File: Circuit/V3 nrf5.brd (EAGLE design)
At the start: 41 x 64.5 mm, 77 parts, among them J4 USB Micro, J7 CORTEX_DEBUG_SMD, Q1 FDV301N, Q2 BSS84, U1 AL8805, U2 MCP73831, U3 BC840M, U4 3.3V/150mA, U5 AL8805, U6 AL8805, U8 TPS61236P, Y1 32.768kHz

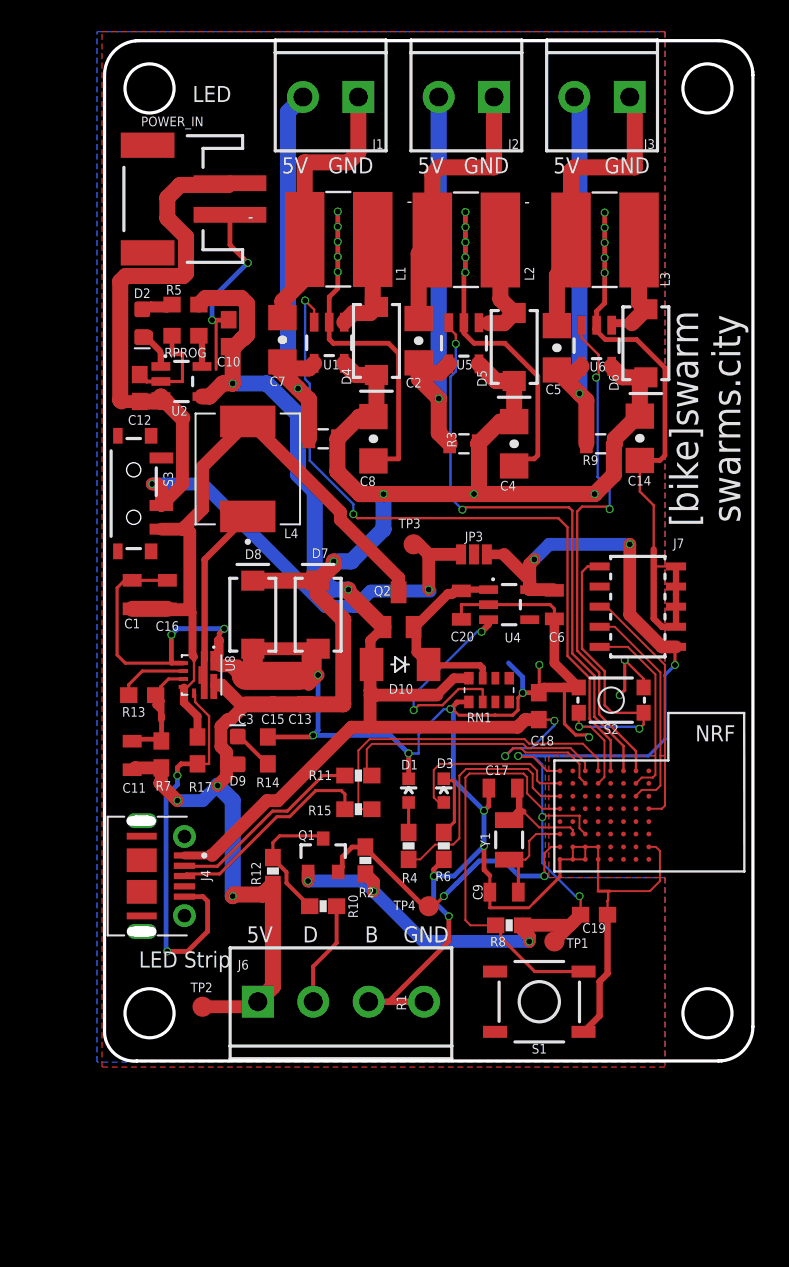
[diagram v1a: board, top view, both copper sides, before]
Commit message: clean traces
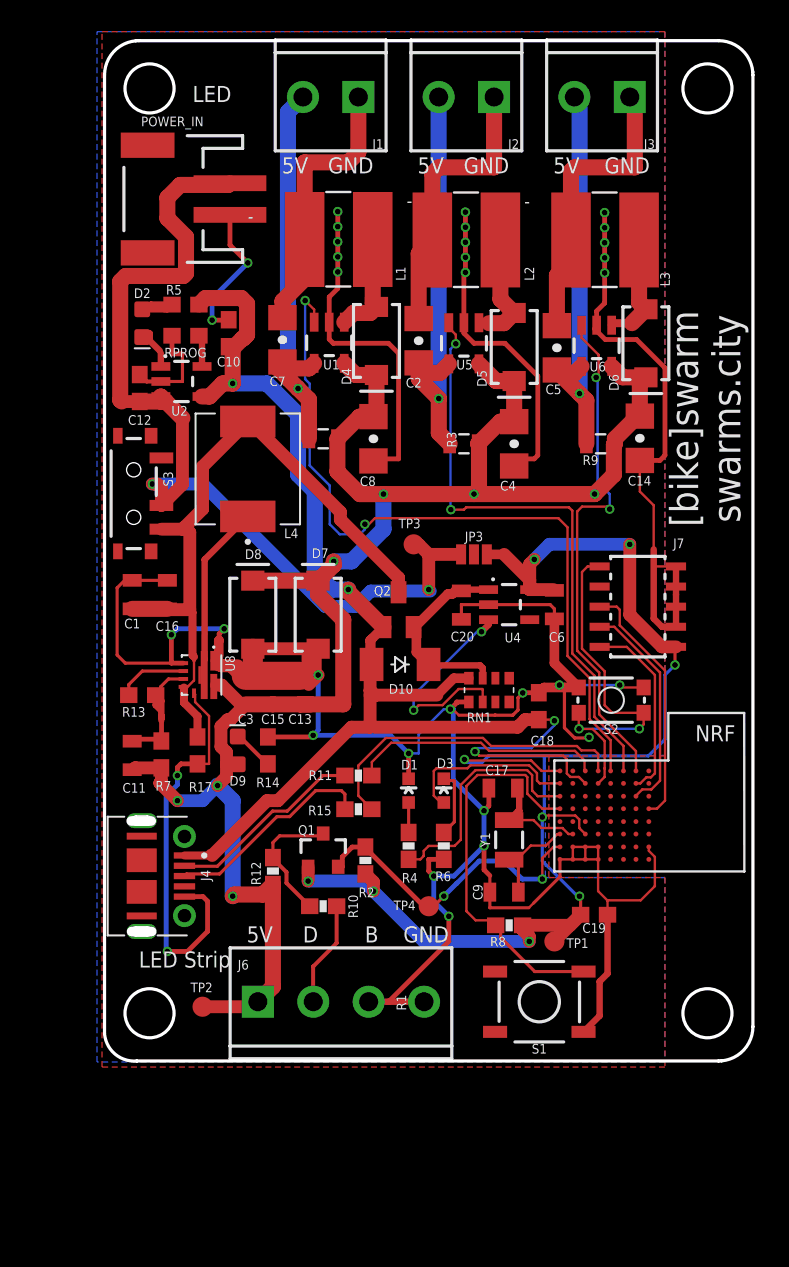
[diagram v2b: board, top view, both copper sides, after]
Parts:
- moved Q1 0.32 mm to (14.0, 13.7)
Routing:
- net GND: track 300.9 -> 292.4 mm, vias 34 -> 33
- net 3.3V: track 81.2 -> 88.0 mm
- net VBUS: track 90.8 -> 94.3 mm
- net CTRL_CH1: track 46.7 -> 49.0 mm
- net SWITCH_1: track 25.9 -> 24.9 mm
- net D+: track 21.3 -> 20.5 mm
- net SWO: track 15.6 -> 16.3 mm
- net LED_2: track 11.9 -> 11.2 mm

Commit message: traces
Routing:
- net VBAT_S: track 65.4 -> 64.7 mm
- net N$3: track 12.8 -> 13.4 mm
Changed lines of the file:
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@@
 <via x="22.0345" y="35.21075" extent="1-16" drill="0.35"/>
 <wire x1="22.0091" y1="35.23615" x2="22.0345" y2="35.21075" width="0.1524" layer="16"/>
-<wire x1="23.00605" y1="35.3568" x2="22.86" y2="35.21075" width="0.1524" layer="1"/>
-<wire x1="22.0345" y1="35.21075" x2="22.86" y2="35.21075" width="0.1524" layer="1"/>
-<wire x1="23.00605" y1="35.3568" x2="29.49500625" y2="35.3568" width="0.1524" layer="1"/>
-<wire x1="29.49500625" y1="35.3568" x2="29.7084" y2="35.14340625" width="0.1524" layer="1"/>
+<wire x1="22.0345" y1="35.21075" x2="29.4005" y2="35.21075" width="0.1524" layer="1"/>
+<wire x1="29.4005" y1="35.21075" x2="29.7084" y2="34.90285" width="0.1524" layer="1"/>
+<wire x1="29.7084" y1="34.90285" x2="29.7084" y2="26.11794375" width="0.1524" layer="1"/>
 <wire x1="29.7084" y1="26.11794375" x2="31.1023" y2="24.72404375" width="0.1524" layer="1"/>
-<wire x1="29.7084" y1="35.14340625" x2="29.7084" y2="26.11794375" width="0.1524" layer="1"/>
 <wire x1="31.1023" y1="22.1230625" x2="31.1023" y2="24.72404375" width="0.1524" layer="1"/>
 <contactref element="U3" pad="A2"/>
@@
 <wire x1="3.7465" y1="18.8985" x2="2.109" y2="18.8985" width="0.8128" layer="1"/>
 <via x="14.63675" y="31.9405" extent="1-16" drill="0.35"/>
-<wire x1="17.78" y1="33.9725" x2="15.748" y2="31.9405" width="1.016" layer="16"/>
-<wire x1="14.63675" y1="31.9405" x2="15.748" y2="31.9405" width="1.016" layer="16"/>
+<wire x1="17.78" y1="33.9725" x2="16.5735" y2="32.766" width="1.016" layer="16"/>
+<wire x1="14.63675" y1="31.9405" x2="14.63675" y2="32.73425" width="1.016" layer="16"/>
+<wire x1="14.6685" y1="32.766" x2="14.63675" y2="32.73425" width="1.016" layer="16"/>
+<wire x1="16.5735" y1="32.766" x2="14.6685" y2="32.766" width="1.016" layer="16"/>
 <wire x1="17.78" y1="33.9725" x2="17.78" y2="36.195" width="1.016" layer="16"/>
 <via x="17.78" y="36.195" extent="1-16" drill="0.35"/>
@@
 <wire x1="6.4565" y1="25.7175" x2="6.4565" y2="27.305" width="0.3048" layer="1"/>
 <wire x1="6.4565" y1="27.305" x2="6.5165" y2="27.365" width="0.3048" layer="1"/>
-<wire x1="9.2075" y1="34.7825" x2="6.4809" y2="32.0559" width="0.4064" layer="1"/>
+<wire x1="9.2075" y1="34.7825" x2="8.255" y2="34.7825" width="0.4064" layer="1"/>
+<wire x1="8.255" y1="34.7825" x2="6.4809" y2="33.0084" width="0.4064" layer="1"/>
 <wire x1="6.4809" y1="25.7419" x2="6.4565" y2="25.7175" width="0.4064" layer="1"/>
-<wire x1="6.4809" y1="32.0559" x2="6.4809" y2="25.7419" width="0.4064" layer="1"/>
+<wire x1="6.4809" y1="33.0084" x2="6.4809" y2="25.7419" width="0.4064" layer="1"/>
 </signal>
 <signal name="N$8">
@@
 <wire x1="1.1494" y1="42.13490625" x2="1.24480625" y2="42.0395" width="0.8128" layer="1"/>
 <wire x1="1.24480625" y1="42.0395" x2="2.386" y2="42.0395" width="0.8128" layer="1"/>
-<wire x1="3.75025" y1="35.47675" x2="3.75025" y2="36.57225" width="0.8128" layer="1"/>
-<wire x1="3.75025" y1="36.57225" x2="3.4925" y2="36.83" width="0.8128" layer="1"/>
-<wire x1="3.4925" y1="36.83" x2="3.175" y2="36.83" width="0.8128" layer="1"/>
-<via x="3.175" y="36.83" extent="1-16" drill="0.35"/>
+<wire x1="3.84175" y1="37.05225" x2="3.75025" y2="36.96075" width="0.8128" layer="1"/>
+<wire x1="3.75025" y1="36.96075" x2="3.75025" y2="35.47675" width="0.8128" layer="1"/>
+<via x="3.84175" y="37.05225" extent="1-16" drill="0.35"/>
 <wire x1="14.09824375" y1="29.0957" x2="15.9993875" y2="29.0957" width="0.8128" layer="16"/>
-<wire x1="3.175" y1="36.83" x2="6.36394375" y2="36.83" width="0.8128" layer="16"/>
+<wire x1="3.84175" y1="37.05225" x2="6.14169375" y2="37.05225" width="0.8128" layer="16"/>
 <wire x1="16.9709375" y1="30.06725" x2="20.73275" y2="30.06725" width="0.8128" layer="16"/>
-<wire x1="6.36394375" y1="36.83" x2="14.09824375" y2="29.0957" width="0.8128" layer="16"/>
+<wire x1="6.14169375" y1="37.05225" x2="14.09824375" y2="29.0957" width="0.8128" layer="16"/>
 <wire x1="15.9993875" y1="29.0957" x2="16.9709375" y2="30.06725" width="0.8128" layer="16"/>
 <wire x1="20.6375" y1="32.385" x2="20.6375" y2="30.1625" width="0.8128" layer="1"/>

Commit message: Updating digikey parts.
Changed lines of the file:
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@@
 <drawing>
 <settings>
-<setting alwaysvectorfont="no"/>
+<setting alwaysvectorfont="yes"/>
 <setting keepoldvectorfont="yes"/>
 <setting verticaltext="up"/>
@@
 <layer number="25" name="tNames" color="7" fill="1" visible="yes" active="yes"/>
 <layer number="26" name="bNames" color="7" fill="1" visible="yes" active="yes"/>
-<layer number="27" name="tValues" color="7" fill="1" visible="no" active="yes"/>
+<layer number="27" name="tValues" color="7" fill="1" visible="yes" active="yes"/>
 <layer number="28" name="bValues" color="7" fill="1" visible="no" active="yes"/>
 <layer number="29" name="tStop" color="7" fill="3" visible="no" active="yes"/>
@@
 </element>
 <element name="R10" library="SparkFun" package="0603-RES" value="330" x="13.97" y="10.16" smashed="yes" rot="R180">
-<attribute name="DIGIKEY" value="A130088CT-ND" x="13.97" y="10.16" size="1.778" layer="27" rot="R180" display="off"/>
+<attribute name="DIGIKEY" value="P330HCT-ND" x="13.97" y="10.16" size="1.778" layer="27" rot="R180" display="off"/>
 <attribute name="NAME" x="15.5575" y="10.89025" size="0.6096" layer="25" font="vector" rot="R270"/>
 <attribute name="VALUE" x="14.986" y="11.303" size="0.4064" layer="27" font="vector" rot="R180"/>
@@
 </element>
 <element name="R15" library="SparkFun" package="0603-RES" value="22" x="16.1925" y="16.28775" smashed="yes">
-<attribute name="DIGIKEY" value="P10KGCT-ND" x="16.1925" y="16.28775" size="1.778" layer="27" display="off"/>
+<attribute name="DIGIKEY" value="A103067TR-ND " x="16.1925" y="16.28775" size="1.778" layer="27" display="off"/>
 <attribute name="NAME" x="13.0175" y="15.90675" size="0.6096" layer="25" font="vector"/>
 <attribute name="VALUE" x="15.1765" y="15.14475" size="0.4064" layer="27" font="vector"/>
@@
 <wire x1="7.374" y1="26.935" x2="7.374" y2="25.9825" width="0.6096" layer="1"/>
 <wire x1="7.374" y1="25.9825" x2="7.0565" y2="25.665" width="0.3048" layer="1"/>
-<wire x1="6.0325" y1="19.1525" x2="4.98475" y2="19.1525" width="0.3048" layer="1"/>
-<wire x1="4.7625" y1="18.415" x2="4.7625" y2="18.93025" width="0.3048" layer="1"/>
-<wire x1="4.98475" y1="19.1525" x2="4.7625" y2="18.93025" width="0.3048" layer="1"/>
-<via x="4.7625" y="18.415" extent="1-16" drill="0.35"/>
-<wire x1="4.7625" y1="18.415" x2="4.7625" y2="17.83329375" width="0.3048" layer="16"/>
-<wire x1="4.7625" y1="17.83329375" x2="4.0513" y2="17.12209375" width="0.3048" layer="16"/>
+<wire x1="6.0325" y1="19.1525" x2="6.0325" y2="15.875" width="0.3048" layer="1"/>
+<via x="6.0325" y="15.875" extent="1-16" drill="0.35"/>
+<wire x1="6.0325" y1="15.875" x2="4.7625" y2="15.875" width="0.3048" layer="16"/>
+<wire x1="4.7625" y1="15.875" x2="4.0513" y2="15.1638" width="0.3048" layer="16"/>
+<wire x1="4.0513" y1="15.1638" x2="4.0513" y2="7.3787" width="0.3048" layer="16"/>
 <via x="4.1275" y="7.3025" extent="1-16" drill="0.35"/>
 <wire x1="4.1275" y1="7.3025" x2="5.3975" y2="7.3025" width="0.3048" layer="1"/>
@@
 <wire x1="6.6675" y1="10.4775" x2="6.38" y2="10.765" width="0.3048" layer="1"/>
 <wire x1="6.38" y1="10.765" x2="5.2075" y2="10.765" width="0.3048" layer="1"/>
-<wire x1="4.0513" y1="17.12209375" x2="4.0513" y2="7.3787" width="0.3048" layer="16"/>
 <wire x1="4.0513" y1="7.3787" x2="4.1275" y2="7.3025" width="0.3048" layer="16"/>
 <wire x1="8.001" y1="47.205" x2="7.9765" y2="47.1805" width="0.3048" layer="1"/>

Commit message: Changing pins to match board.
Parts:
- U4: value 3.3V/150mA -> MIC5205
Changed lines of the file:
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@@
 <attribute name="VALUE" x="21.87575" y="27.84475" size="1.27" layer="27" rot="R180"/>
 </element>
-<element name="U4" library="SparkFun-IC-Power" library_urn="urn:adsk.eagle:library:526" package="SOT23-5" package3d_urn="urn:adsk.eagle:package:39060/1" value="3.3V/150mA" x="25.7175" y="29.21" smashed="yes" rot="R270">
+<element name="U4" library="SparkFun-IC-Power" library_urn="urn:adsk.eagle:library:526" package="SOT23-5" package3d_urn="urn:adsk.eagle:package:39060/1" value="MIC5205" x="25.7175" y="29.21" smashed="yes" rot="R270">
 <attribute name="DIGIKEY" value="576-1259-1-ND" x="25.7175" y="29.21" size="1.778" layer="27" rot="R270" display="off"/>
 <attribute name="NAME" x="25.43175" y="26.82875" size="0.6096" layer="25"/>

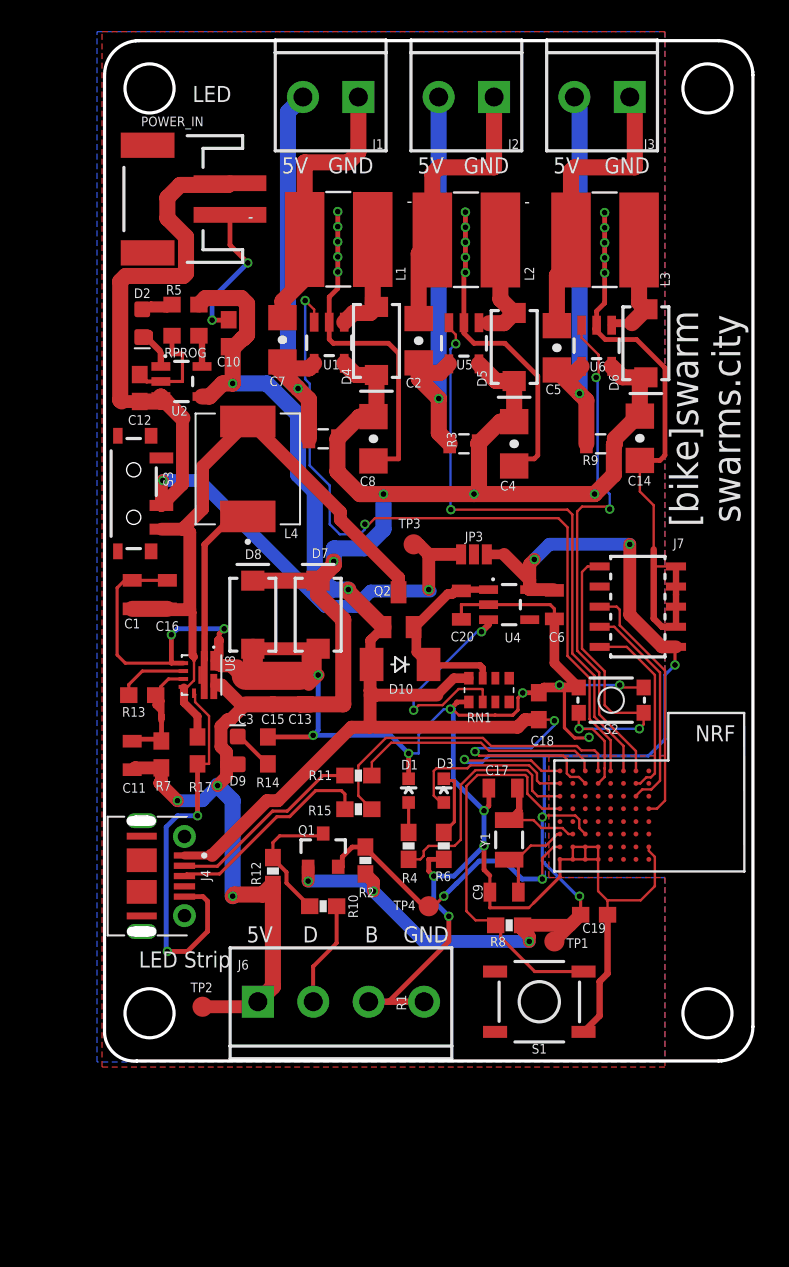
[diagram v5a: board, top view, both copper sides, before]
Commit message: Removing picobuck, touching up and finalizing schematic layout, switching to neopixel 3W led (headlamp). Needs new dimensions to fit with battery in enclosure.
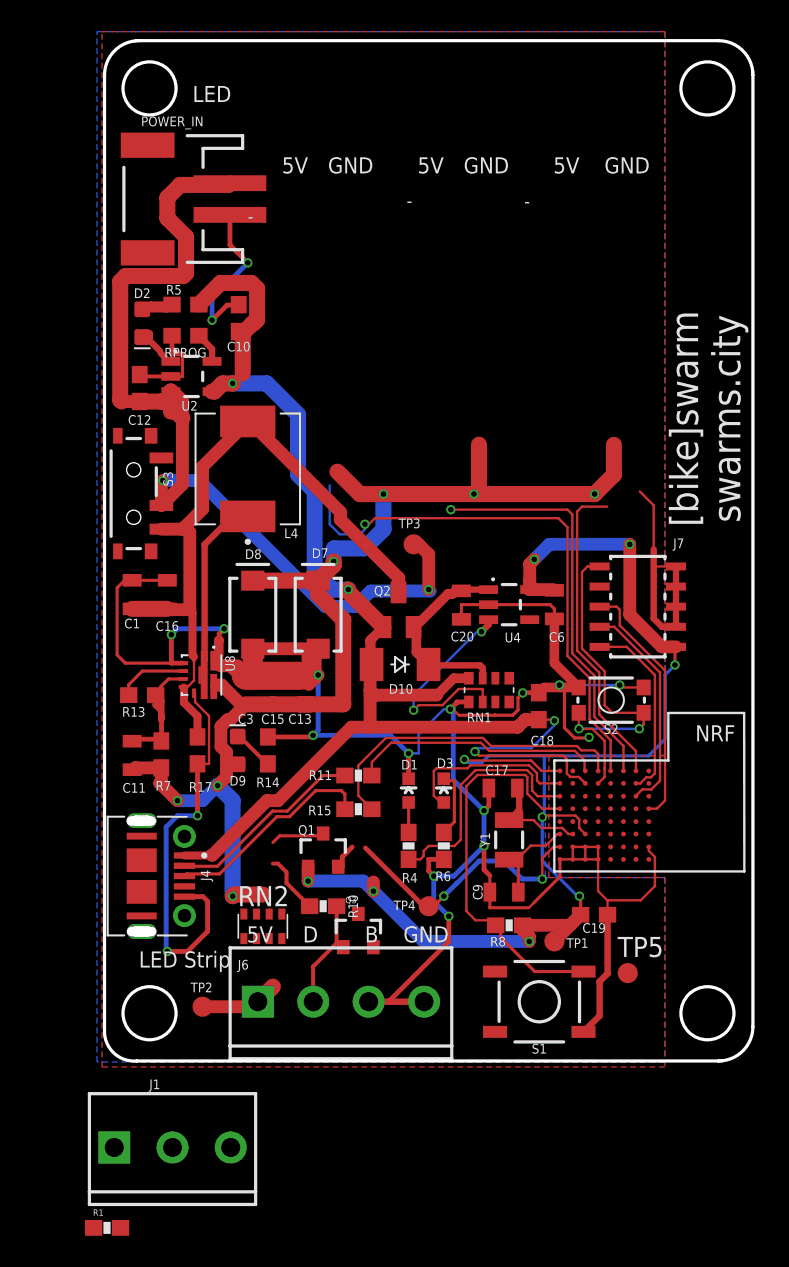
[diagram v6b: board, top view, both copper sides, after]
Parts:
- removed C14, C4, C8: 2.2uF, SparkFun-Capacitors:1206-CAP
- removed C2, C5, C7: 1uF, SparkFun-Capacitors:1206-CAP
- removed D4, D5, D6: 3A/40V/500mV, SparkFun-DiscreteSemi:SMA-DIODE
- removed J2, J3: (no value), SparkFun-Connectors:SCREWTERMINAL-3.5MM-2
- removed JP3: JUMPER-SMT_3_1-NC, SparkFun-Jumpers:SMT-JUMPER_3_1-NC_PASTE_NO-SILK
- removed L1, L2, L3: 33uH, SparkFun-Passives:SRN6045
- removed R12, R2: 10K, SparkFun:0603-RES
- removed R3, R9: 0.3R, SparkFun-Resistors:0805
- removed U1, U5, U6: AL8805, SparkFun-PowerIC:SOT23-5
- added Q3: FDV301N, SparkFun:SOT23-3
- added RN2: (no value), resistor-dil:EXBV8V
- added TP5: TPSB1,27, testpad:B1,27
- C1, C11: value 10uF -> 22uF
- C16, C6: value 1uF -> 22uF
- J1: device SparkFun-Connectors:SCREWTERMINAL-3.5MM-2 -> SparkFun-Connectors:SCREWTERMINAL-3.5MM-3_LOCK.007S
- R1: value 0.3R -> 330; device SparkFun-Resistors:0805 -> SparkFun:0603-RES
- R13: value 294k -> 100k
- R17, R7: device SparkFun-Resistors:0603 -> SparkFun-Resistors:0603@1
- moved J1 68.1 mm to (0.95, -5.08), turned to 0 degrees
- moved R1 51.7 mm to (0.32, -10.2), turned to 0 degrees
- moved C10 1.14 mm to (8.64, 47.3)
- moved U2 0.71 mm to (5.65, 43.6)
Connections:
- removed net OUT1+: C7.1, J1.2, R1.2, U1.4
- removed net OUT1-: C7.2, J1.1, L1.2
- removed net OUT2+: C2.1, J2.2, R3.2, U5.4
- removed net OUT2-: C2.2, J2.1, L2.2
- removed net OUT3+: C5.1, J3.2, R9.2, U6.4
- removed net OUT3-: C5.2, J3.1, L3.2
- removed net SW: D4.A, L1.1, U1.1
- removed net SW1: D5.A, L2.1, U5.1
- removed net SW2: D6.A, L3.1, U6.1
- new net HEADLAMP_3V3: Q3.2, RN2.2, TP5.TP, U3.G1
- new net HEADLAMP_5V: Q3.3, R1.2, RN2.4
- new net N$17: J1.2, R1.1
- net 3.3V: now also Q3.1, RN2.7, RN2.8; no longer JP3.3, R2.1
- net 5V: now also J1.3, RN2.5, RN2.6; no longer C14.1, C4.1, C8.1, D4.C, D5.C, D6.C, R1.1, R12.1, R3.1, R9.1, U1.5, U5.5, U6.5
- net CTRL_CH1: no longer U1.3
- net CTRL_CH2: no longer U5.3
- net CTRL_CH3: no longer U6.3
- net GND: now also J1.1; no longer C14.2, C4.2, C8.2, U1.2, U5.2, U6.2
- net STRIP_3V3: now also RN2.1; no longer R2.2
- net STRIP_5V: now also RN2.3; no longer R12.2
- net VBAT_S: no longer JP3.1
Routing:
- net GND: track 292.6 -> 229.3 mm, vias 33 -> 18
- net 5V: track 116.1 -> 83.0 mm
- net OUT2+: track 27.4 -> 0.00 mm, vias 1 -> 0
- net OUT1+: track 27.2 -> 0.00 mm, vias 1 -> 0
- net OUT3+: track 26.0 -> 0.00 mm, vias 1 -> 0
- net OUT3-: track 19.0 -> 0.00 mm
- net OUT2-: track 18.0 -> 0.00 mm
- net OUT1-: track 17.8 -> 0.00 mm
- net CTRL_CH1: track 49.0 -> 35.1 mm, vias 2 -> 1
- net CTRL_CH3: track 32.7 -> 19.9 mm, vias 2 -> 0
- net CTRL_CH2: track 37.5 -> 25.4 mm, vias 2 -> 1
- net SW1: track 7.52 -> 0.00 mm
- net SW2: track 7.43 -> 0.00 mm
- net SW: track 6.79 -> 0.00 mm
- net 3.3V: track 88.0 -> 83.9 mm
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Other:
- outline, holes or cut-outs redrawn
